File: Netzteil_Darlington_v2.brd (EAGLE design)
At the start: 155.7 x 120 mm, 155 parts, among them IC10 LT4320DIL08, IC11 OPA2197, IC13 OPA2197, IC15 LD33V, IC17 7815TV, IC2 OPA2197, IC4 VXO78012-1000, IC5 LD33V, IC6 VXO7805-1000, IC7 MCP4922, IC8 LTC6102HMS8#PBF, IC9 LM334, T1 IRLL110TRPBF, T10 BC847ALT1G, T11 BC847ALT1G, T12 DMG2302UK-7, T13 DMG2302UK-7, T14 DMG2302UK-7, T2 BC847ALT1G, T3 BD139, T4 2N5401, T5 TIP3055, T6 TIP3055, T7 BD139, T8 BC847ALT1G

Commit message: update to latest version
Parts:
- removed C44: 10µ / C3216X7R1E106M160AB, goujine:1206
- removed C46: 100n, goujine:0805
- removed CRNT_READ: (no value), jumper:JP2
- removed D11: EDZV13B, neumluc:SOD-523
- removed D13: 1N4007, diode:DO214AA
- removed R25: 347k 1%, neumluc:C0805K
- removed R46: 10k, neumluc:C0805K
- removed T8: BC847ALT1G, neumluc:SOT23-BEC
- added C10, C17: 100n/16V, goujine:C0603K
- added C14, C18, C41: 1µ/16V, goujine:0805
- added C21: 330n, goujine:0805
- added C28: 100n, goujine:0805
- added C32, C37: 1µ/50V, goujine:0805
- added C34: 10µ/16V, goujine:0805
- added C40: 100n/50V, goujine:0805
- added IC1: NCP718BSN330T1G, neumluc:SOT23-5
- added IC12: REF5040, neumluc:MSOP8-0.65-3X3MM
- added IC18, IC19: ADS1015, SparkFun-IC-Conversion:MSOP10
- added L6, L8: MPZ2012S601AT000, neumluc:C0805K
- added R13: 10k, neumluc:C0603K
- added R17: 2k2, neumluc:C0805K
- added R19: 1.27R, neumluc:C0805K
- C22, C29: device goujine:0805 -> goujine:C0603K
- C35: value 100n -> 1µ/50V
- C36: value 100n -> 1µ/16V
- C45: value 10µ / C3216X7R1E106M160AB -> 1µ/16V; device goujine:1206 -> goujine:0805
- C7: value 470n -> 100n/16V; device goujine:0805 -> goujine:C0603K
- C8: value 100n -> 10µ/16V
- C9: value 10µ / C3216X7R1E106M160AB -> 100n/16V; device goujine:1206 -> goujine:C0603K
- D4: value MMSD4148T1G opt -> 1N4007; device adafruit:SOD-123 -> diode:DO214AA
- IC17: value 7815TV -> 7818TV
- IC3: value (none) -> DAC8311; device neumluc:SOT23 -> neumluc:SC-70-6
- IC5: value LD33V -> 7815TV; device neumluc:TO220V -> linear:TO220V
- IC7: value MCP4922 -> DAC8311; device neumluc:TSSOP14 -> neumluc:SC-70-6
- IC9: value LM334 -> NCP718BSN330T1G; device neumluc:TO92-G -> neumluc:SOT23-5
- R1: value 1M -> 2k2 5%; device neumluc:C0603K -> neumluc:C0805K
- R12: value 10R 1% -> 10k; device neumluc:C0805K -> neumluc:C0603K
- R2: value 2.4k 0.1% PCF0805-13-2K4BT1 -> 10k 0.1% 10ppm
- R3: value 12k 0.1% ERA-6ARW123V -> 30k 0.1% 10ppm
- R4, R6: value 220R -> 10k; device neumluc:C0805K -> neumluc:C0603K
- R42: value 681k 1% -> 390k 1%; device neumluc:C0603K -> neumluc:C0805K
- T4: value 2N5401 -> DMMT5551-7-F; device neumluc:TO92-G -> neumluc:SOT-26
- moved R6 80.9 mm to (65.2, 39.6), turned to 0 degrees
- moved R4 62.8 mm to (64.3, 41.0)
- moved R1 40.4 mm to (115.7, 57.3), turned to 90 degrees
- moved T4 37.0 mm to (114.8, 61.4), turned to 90 degrees
- moved D4 22.2 mm to (51.3, 60.4), turned to 270 degrees
- moved C25 18.6 mm to (104.6, 61.5)
- moved C26 18.6 mm to (92.7, 54.4)
- moved C47 18.6 mm to (92.9, 51.0)
- moved C48 18.6 mm to (92.4, 61.5)
- moved IC11 18.6 mm to (97.5, 57.7)
- moved R14 18.6 mm to (106.8, 61.5)
- moved R15 18.6 mm to (102.7, 61.5)
- moved R32 18.6 mm to (90.5, 61.5)
- moved R35 18.6 mm to (97.5, 61.6)
- moved R37 18.6 mm to (95.9, 51.9)
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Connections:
- removed net AREF2048: C9.1, IC3.2, IC7.11, IC7.13, U$33.AREF
- removed net CRNT_READ_OP: CRNT_READ.2, IC13.5
- removed net DAC_CS: IC7.3, U$33.14/A0
- removed net DAC_SHDN: IC7.9, U$33.A22/DAC1
- removed net MISO: U$33.12/MISO
- removed net N$39: C44.2, D13.A, IC5.2, L5.1
- new net +27V: C1.+, C12.2, C19.2, C2.+, C21.1, C27.1, C42.1, C53.1, D4.C, D9.C, IC10.6, IC17.1, IC4.1, IC5.1, IC6.1, IC8.7, R5.I2, T15.3, T16.3
- new net +3.3V_A2: C14.2, IC9.5, L6.2
- new net +3.3V_LP: R4.2, R6.1, U$33.3V3_LO
- new net IDAC_CS: IC7.1, U$33.15/A1
- new net N$18: IC19.2, R12.2
- new net N$24: C17.1, IC18.1, IC18.8, L8.1, R13.1
- new net N$25: C37.2, C40.2, IC12.2, L5.1
- new net N$32: C45.1, R19.2
- new net SCL: IC18.10, IC19.10, R4.1, U$33.19/A5/SCL
- new net SDA: IC18.9, IC19.9, R6.2, U$33.18/A4/SDA
- new net VDAC_CS: IC3.1, U$33.14/A0
- new net VREF4096: C34.1, C41.1, C7.1, C8.1, C9.1, IC12.6, IC3.4, IC7.4, R19.1
- net +15V: now also C28.1, C32.2, C35.2, D4.A, IC1.1, IC1.3, IC9.1, IC9.3, L5.2, R1.1, R17.1; no longer C22.1, C29.1, C35.1, C43.1, D13.C, D9.A, IC13.8, IC17.3, IC2.8, R18.1, R46.1, T11.C
- net +18V: now also C22.1, C29.1, C43.1, D9.A, IC13.8, IC17.3, IC2.8, R18.1, T11.C; no longer C1.+, C12.2, C19.2, C2.+, C27.1, C42.1, C53.1, D9.C, IC10.6, IC17.1, IC4.1, IC6.1, IC8.7, R5.I2, T15.3, T16.3
- net +3.3V_A: now also C18.2, IC1.5, L8.2; no longer C36.2, C45.1, C46.1, C7.1, C8.1, IC3.1, IC7.1, L5.2
- net +V_ADJ: now also T4.4; no longer IC9.1, T8.C
- net ADC_CH0: now also IC18.6; no longer U$33.20/A6
- net ADC_CH1: now also IC19.4; no longer U$33.33/A14
- net ADC_CH2: now also IC19.6; no longer U$33.34/A15
- net ADC_CH3: now also IC18.4; no longer U$33.19/A5/SCL
- net AGND: now also C10.2, C14.1, C17.2, C18.1, C21.2, C28.2, C32.1, C34.2, C35.1, C36.2, C37.1, C40.1, C41.2, IC1.2, IC12.4, IC18.3, IC18.5, IC18.7, IC19.1, IC19.3, IC19.5, IC19.7, IC3.5, IC5.2, IC7.5, IC9.2, R17.2, SENSE.1, T4.5, T4.6; no longer C35.2, C36.1, C44.1, C46.2, D11.A, IC3.3, IC5.1, IC7.12, IC7.8, IC9.3, R1.1, R12.2, T8.E
- net BTN_I_DOWN: now also U$33.37/A18; no longer U$33.39/A20
- net BTN_I_UP: now also U$33.36/A17; no longer U$33.38/A19
- net BTN_V_DOWN: now also U$33.35/A16; no longer U$33.37/A18
- net BTN_V_UP: now also U$33.34/A15; no longer U$33.36/A17
- net CRNT_READ: now also IC13.5; no longer CRNT_READ.3
- net CRNT_READ_RAW: no longer CRNT_READ.1
- net ISET: now also IC7.6; no longer IC7.14
- net MOSI: now also IC3.3, IC7.3; no longer IC7.5
- net N$10: no longer D4.C
- net N$11: now also R1.2, T4.1, T4.2, T4.3; no longer R25.1, T8.B
- net N$14: now also C36.1, IC12.5; no longer D11.C, R25.2, R46.2
- net N$15: no longer R4.2
- net N$16: now also IC18.2, R13.2; no longer IC9.2, R12.1
- net N$19: now also C10.1, IC19.8, L6.1, R12.1; no longer R1.2, T4.2
- net N$21: no longer T4.1
- net N$22: no longer D4.A, T4.3
- net N$4: no longer R6.1
- net N$5: no longer R6.2
- net N$8: no longer R4.1
- net SCK: now also IC3.2, IC7.2; no longer IC7.4
- net TH0: now also U$33.33/A14; no longer U$33.35/A16
- net VSET: now also IC3.6; no longer IC7.10
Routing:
- net +27V: track 0.00 -> 188.7 mm, vias 0 -> 86
- net +18V: track 159.4 -> 50.0 mm, vias 85 -> 2
- net SCL: track 0.00 -> 68.0 mm
- net SDA: track 0.00 -> 65.3 mm
- net AREF2048: track 38.4 -> 0.00 mm
- net +3.3V_A: track 40.2 -> 3.80 mm, vias 2 -> 0
- net +V_ADJ: track 21.1 -> 54.8 mm
- net VREF4096: track 0.00 -> 22.2 mm
- net AGND: track 87.5 -> 109.3 mm, vias 34 -> 45
- net N$8: track 23.7 -> 5.19 mm, vias 1 -> 0
- net SCK: track 28.8 -> 47.3 mm
- net N$4: track 23.7 -> 5.19 mm, vias 1 -> 0
- net TH0: track 46.5 -> 64.8 mm, vias 6 -> 4
- net +15V: track 171.3 -> 153.4 mm, vias 9 -> 10
- net VDAC_CS: track 0.00 -> 17.9 mm, vias 0 -> 2
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- added copper zone on layer 1, net +27V
- added copper zone on layer 16, net +27V
- removed copper zone on layer 1, net +18V
- removed copper zone on layer 16, net +18V
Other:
- board size 155.7 x 120 mm -> 156 x 120 mm
- board text removed: "HS: ATS-52350P-C1-R0 ATS-54350R-C1-R0"

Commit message: update to latest version
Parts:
- removed BTNS: (no value), con-lstb:MA05-1
- added I: (no value), con-lstb:MA03-1
- added SENSE_GND, V: (no value), jumper:JP1
- moved H4 46.1 mm to (135.8, 67.3)
- moved VOUT 39.2 mm to (113.4, 53.8)
- moved GND_OUT_CON 30.9 mm to (135.0, 53.8)
- moved D6 26.5 mm to (110.9, 67.1), turned to 180 degrees
- moved REL1 23.8 mm to (124.2, 48.7)
- moved D8 23.7 mm to (124.0, 32.1)
- moved R1 22.7 mm to (98.0, 71.5), turned to 270 degrees
- moved T1 22.1 mm to (120.4, 24.8), turned to 180 degrees
- moved R31 20.8 mm to (123.7, 20.9), turned to 270 degrees
- moved VSS 18.4 mm to (47.4, 2.73)
- moved C16 17.8 mm to (120.7, 9.63)
- moved IC4 17.8 mm to (125.3, 8.52)
- moved L4 17.8 mm to (125.3, 14.2)
- moved T4 16.9 mm to (99.0, 67.3), turned to 270 degrees
- moved H3 16.6 mm to (135.8, 19.7)
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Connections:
- new net SENSE_GND: IC19.5, SENSE_GND.1, SENSE_GND.2
- net +V_ADJ: now also REL1.S1; no longer REL1.P1
- net AGND: now also I.3, REL1.S2; no longer BTNS.5, IC19.5, REL1.P2, SENSE.1
- net BTN_I_DOWN: now also I.2, U$33.17/A3; no longer BTNS.4, U$33.37/A18
- net BTN_I_UP: now also I.1, U$33.16/A2; no longer BTNS.3, U$33.36/A17
- net BTN_V_DOWN: now also V.2; no longer BTNS.2
- net BTN_V_UP: now also V.1; no longer BTNS.1
- net GND_OUT_CON: now also REL1.P2; no longer REL1.S2
- net SENSE: now also SENSE.1
- net V_OUT_CON: now also REL1.P1; no longer REL1.S1
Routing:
- net REL-OUT: track 47.9 -> 25.2 mm
- net +12V: track 55.4 -> 36.0 mm
- net +27V: track 188.7 -> 173.2 mm
- net N$22: track 74.6 -> 63.1 mm
- net TH0: track 64.8 -> 53.4 mm
- net SENSE_GND: track 0.00 -> 11.1 mm
- net SCL: track 68.0 -> 59.3 mm
- net SDA: track 65.3 -> 57.6 mm
- net BTN_V_DOWN: track 3.57 -> 11.1 mm
- net +V_ADJ: track 54.8 -> 61.2 mm
- net +15V: track 153.4 -> 147.4 mm
- net VDAC_CS: track 17.9 -> 13.0 mm
- net IDAC_CS: track 17.7 -> 12.8 mm
- net N$37: track 4.30 -> 8.90 mm
- net N$5: track 41.3 -> 36.8 mm
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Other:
- board size 156 x 120 mm -> 141 x 115.5 mm

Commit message: Update to v1.9
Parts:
- removed C29: 100n, goujine:C0603K
- removed C50: 10n, goujine:0805
- removed D12: 1N4007, diode:DO214AA
- removed DSPLY2, LED, SENSE, SENSE_GND, V: (no value), jumper:JP1
- removed DSPLY_LED: (no value), neumluc:MA03-1
- removed ESP: (no value), con-lstb:MA06-1
- removed I: (no value), con-lstb:MA03-1
- removed IC11, IC13: OPA2197, goujine:SOP8
- removed R15: 10.1k 0.1% RN732ATTD1012B25, neumluc:C0805K
- removed R31: 360R, neumluc:C0805K
- removed R38: 4.7k, neumluc:C0805K
- removed R39: 100R, neumluc:C0805K
- removed T10: BC847ALT1G, neumluc:SOT23-BEC
- added BTN, SV1, SV2: (no value), neumluc:JST-PH-2.0-2P
- added C33, C44: 100µ/50V, goujine:C+/3.5/8
- added ESP/BTNS: (no value), neumluc:JST-PH-2.0-8P
- added IC14: QUAD-OPVOPA4197, neumluc:SO14
- added KK2: D01S, heatsink:D01S
- added R25, R26: 1k 1% 1/8W, neumluc:C0805K
- added SINK: (no value), jumper:JP1
- added SV5: (no value), neumluc:JST-PH-2.0-5P
- C1, C2: value UVZ1H103MRD -> 10000µ/50V
- C10, C17, C7, C9: device goujine:C0603K -> goujine:0805
- C11: value 330n opt -> 330n opt/50V
- C13: value 100n opt -> 100n opt/50V
- C15: value 100µ/50V EEU-FR1H101 -> 100µ/50V
- C16: value 10µ/16V -> 10µ/25V; device we-rcl:C1210 -> goujine:1206
- C20: device we-rcl:C1210 -> goujine:1206
- C21, C42: value 330n -> 330n/50V
- C22: value 100n -> 100n/35V; device goujine:C0603K -> goujine:0805
- C23, C30, C39, C49: value 10µ / C3216X7R1E106M160AB -> 10µ/16V
- C24, C3, C31, C38, C48: value 100n -> 100n/16V
- C25, C28, C43: value 100n -> 100n/35V
- C26: value 100n -> 1n/50V
- C27: value 100n -> 100n/50V
- C32, C35, C37: value 1µ/50V -> 1µ/35V
- C34, C8: device goujine:0805 -> goujine:1206
- C4: value 10n -> 10n/50V
- C40: value 100n/50V -> 100n/35V
- C47, C51: value 10n -> 10n/16V
- C5: value 1n -> 1n/50V
- C52: value 22p opt -> 22p opt/35V C0G
- C53: value (none) -> 1µ/50V
- C6: value 22pF -> 22pF/35V C0G
- D14, D6: value CDBA5200-HF -> CGRB307-G; device neumluc:DO214AC-2 -> neumluc:DO214AA-CGRB307-G
- D4, D8, D9: value 1N4007 -> CGRB307-G; device diode:DO214AA -> neumluc:DO214AA-CGRB307-G
- DSPLY: device con-lstb:MA07-1 -> neumluc:JST-PH-2.0-7P
- ENC: device con-lstb:MA03-1 -> neumluc:JST-PH-2.0-3P
- FAN: device con-lstb:MA04-1 -> neumluc:JST-PH-2.0-4P
- IC18, IC19: value ADS1015 -> ADS1115; device SparkFun-IC-Conversion:MSOP10 -> neumluc:MSOP10
- IC2: value OPA2197 -> (none)
- R1: value 2k2 5% -> 12k 0.5% 50 ppm 1/10W
- R10: value 4.7k opt -> 4.7k opt 1% 1/10W
- R11, R16: value 22R -> 22R 5% 1/10W
- R12: value 10k -> 221R 0.5% 50ppm 1/10W; device neumluc:C0603K -> neumluc:C0805K
- R13: value 10k -> 1k 0.5% 50 ppm 1/10W; device neumluc:C0603K -> neumluc:C0805K
- R14: value 90.9k 0.1% RN73C2A90K9BTDF -> 10R 0.5% 50 ppm 1/4W
- R17: value 2k2 -> 2k2 5% 1/8W
- R18: value 2k2 -> 1k 1% 1/8W
- R19: value 1.27R -> 1.27R 1% 1/10W
- R20, R21: value 0R1 0.5% -> 0R1 0.5% 7W
- R22, R32: value 10.1k 0.1% RN732ATTD1012B25 -> 10.1k 0.1% 10ppm 1/10W
- R23, R30: value 90.9k 0.1% RN73C2A90K9BTDF -> 90.9k 0.1% 10ppm 1/10W
- R24: value 1k opt -> 1k 1% 1/10W
- R28, R29: value 220R -> 220R 5% 1/10W
- R35, R40: value 4.7k -> 4.7k 5% 1/10W
- R37: value 100R -> 2.2k 5% 1/8W
- R4, R6: value 10k -> 10k 5% 1/10W; device neumluc:C0603K -> neumluc:C0805K
- R41: value 100R -> 100R 5% 1/10W
- R42: value 390k 1% -> 65k 1% 1/10W
- R43: value 5k 0.1% low ppm TNPW12065K00BEEN -> 5k 0.1% 25ppm
- R44, R45: value 100R 0.1% low ppm PCF0805-13-100RBT1 -> 100R 0.1% 5ppm 1/10W
- R48, R7: value 10k -> 10k 5% 1/10W
- R5: value 10m -> 10m 0.1% 15ppm 0.5W
- R8: value 47k -> 47k 1% 1/10W
- R9: value 4.7k -> 4.7k 1% 1/10W
- T1: value IRLL110TRPBF -> PMV130ENEAR; device goujine:SOT223-4 -> neumluc:SOT23
- T12, T13, T14: value DMG2302UK-7 -> PMV130ENEAR
- T15, T16, T17, T18: value (none) -> IRFR7546TRPBF
- T4: value DMMT5551-7-F -> PMV130ENEAR; device neumluc:SOT-26 -> neumluc:SOT23
- moved R13 35.2 mm to (97.9, 54.3), turned to 270 degrees
- moved VSS 35.1 mm to (82.3, 5.74)
- moved C32 26.1 mm to (81.3, 45.7)
- moved R1 21.6 mm to (97.2, 49.8), turned to 90 degrees
- moved IC9 20.5 mm to (84.0, 44.9), turned to 180 degrees
- moved C13 20.3 mm to (102.6, 56.5), turned to 270 degrees
- moved C25 19.6 mm to (83.3, 50.6), turned to 180 degrees
- moved D14 16.8 mm to (111.9, 66.1)
- moved C14 15.1 mm to (86.7, 44.3), turned to 270 degrees
- moved IC2 15.0 mm to (87.2, 54.3)
- moved AGND 14.9 mm to (129.5, 59.1)
- moved T4 14.0 mm to (94.9, 54.0), turned to 0 degrees
- moved C42 13.4 mm to (43.0, 62.5), turned to 270 degrees
- moved C22 12.9 mm to (62.1, 67.0), turned to 90 degrees
- moved D6 12.7 mm to (106.1, 55.3), turned to 270 degrees
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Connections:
- removed net ADC_CH1: C50.1, IC19.4, R39.2
- removed net ADC_SENSE: C25.1, IC11.3, R14.1, R15.2
- removed net N$12: D8.A, REL1.+, T1.2, T1.4
- removed net N$37: R31.1, R48.2, T1.1
- removed net N$40: IC11.7, T2.B
- removed net N$42: IC11.1, T10.B
- removed net N$43: IC11.2, R38.1, R39.1, T10.E
- removed net N$44: IC13.7, T11.B
- removed net SENSE: R14.2, SENSE.1, SENSE.2
- removed net SENSE_GND: IC19.5, SENSE_GND.1, SENSE_GND.2
- new net 3.3V_A2_FILTERED: C10.1, IC19.8, L6.1, R1.1, SV1.2
- new net 3.3V_TH: R42.1, SV2.2
- new net N$26: R18.2, R25.1
- new net N$30: R25.2, R26.1
- new net N$31: C6.1, IC14.9, R2.2, R3.2, R8.2
- new net N$33: C26.1, IC2.1, T4.1
- new net N$34: SINK.2, T4.3
- new net N$38: D8.A, REL1.+, T1.3
- new net TH0_ADC: IC19.4, SV1.1
- net +15V: now also C25.1, IC2.8; no longer C26.1, IC11.8, R1.1, R42.1, T10.C
- net +18V: now also IC14.4; no longer C29.1, IC13.8, IC2.8
- net +27V: now also C33.+, C44.+
- net +3.3V: now also DSPLY.6, ESP/BTNS.4; no longer DSPLY.2, DSPLY2.2, ESP.4
- net +5V_INT_D: no longer D12.C
- net +V_ADJ: now also SINK.1; no longer T4.4
- net ADC_CH0: now also IC18.4; no longer IC18.6
- net ADC_CH3: now also IC18.6; no longer IC18.4
- net ADC_VOUT: now also IC2.5; no longer IC11.5
- net AGND: now also IC14.11, R12.2, R14.2, R26.2, U$33.GND2; no longer C26.2, C29.2, C50.2, I.3, IC11.4, IC13.4, R15.1, R18.2, R38.2, T4.5, T4.6
- net BTN_I_DOWN: now also BTN.2; no longer I.2
- net BTN_I_UP: now also BTN.1; no longer I.1
- net BTN_V_DOWN: now also ESP/BTNS.8, U$33.33/A14; no longer U$33.35/A16, V.2
- net BTN_V_UP: now also ESP/BTNS.7; no longer V.1
- net CRNT_READ: now also IC14.13, IC14.5; no longer IC13.5, IC2.6
- net DSPLY_CS: now also DSPLY.1; no longer DSPLY.7
- net DSPLY_DC: now also DSPLY.5; no longer DSPLY.3
- net DSPLY_RST: now also DSPLY.2; no longer DSPLY.6
- net ESP-IO: now also ESP/BTNS.5, U$33.35/A16; no longer ESP.5, U$33.10/CS
- net ESP-RST: now also ESP/BTNS.3; no longer ESP.3
- net ESP-RX: now also ESP/BTNS.2, U$33.32/A13; no longer ESP.2, U$33.31/A12
- net ESP-TX: now also ESP/BTNS.1, U$33.31/A12; no longer ESP.1, U$33.32/A13
- net ISET: now also IC14.12; no longer IC2.5
- net MOSI: now also DSPLY.3; no longer DSPLY.5
- net N$11: now also IC2.3, R12.1; no longer T4.1, T4.2, T4.3
- net N$16: now also R14.1, T4.2; no longer IC18.2
- net N$18: now also C26.2, IC2.2, R13.1; no longer IC19.2, R12.2
- net N$19: now also IC2.7, T2.B; no longer C10.1, IC19.8, L6.1, R12.1
- net N$20: now also SV5.1; no longer LED.1
- net N$21: now also IC14.8; no longer IC2.1
- net N$23: now also SV5.2; no longer LED.2
- net N$24: no longer R13.1
- net N$35: no longer D12.A
- net N$41: now also IC2.6; no longer IC11.6
- net N$45: now also IC14.6; no longer IC13.6
- net N$46: now also SV5.4; no longer DSPLY_LED.2
- net N$48: now also SV5.5; no longer DSPLY_LED.3
- net N$6: now also IC14.7, T11.B; no longer C6.1, IC2.2, R2.2, R3.2, R8.2
- net N$7: now also SV5.3; no longer DSPLY_LED.1
- net OVRCRNT_DET: now also IC14.14, IC14.3; no longer IC13.3, IC2.7
- net OVRCRNT_DET_BUF: now also IC14.1, IC14.2; no longer IC13.1, IC13.2
- net REL-OUT: now also R48.2, T1.1; no longer R31.2
- net TH0: now also SV2.1; no longer U$33.33/A14
- net VSET: now also IC14.10; no longer IC2.3
- net VSS: now also C33.-, C44.-, DSPLY.7, ESP/BTNS.6, T1.2; no longer DSPLY.1, DSPLY2.1, ESP.6, T1.3
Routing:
- net +15V: track 147.4 -> 65.7 mm, vias 10 -> 4
- net TH0: track 53.4 -> 9.82 mm, vias 4 -> 0
- net ESP-IO: track 49.1 -> 18.1 mm
- net +27V: track 173.2 -> 144.7 mm
- net +V_ADJ: track 61.2 -> 33.7 mm
- net +18V: track 48.3 -> 28.6 mm
- net AGND: track 107.8 -> 89.3 mm, vias 44 -> 46
- net 3.3V_A2_FILTERED: track 0.00 -> 18.2 mm
- net N$43: track 13.6 -> 0.00 mm
- net N$22: track 63.1 -> 50.8 mm, vias 2 -> 0
- net N$11: track 4.22 -> 15.6 mm
- net SENSE_GND: track 11.1 -> 0.00 mm
- net N$3: track 70.3 -> 59.3 mm
- net CRNT_READ: track 28.7 -> 18.7 mm
- net N$12: track 8.91 -> 0.00 mm
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- added copper zone on layer 1, net AGND
- added copper zone on layer 1, net CRNT_READ
- added copper zone on layer 1, net CRNT_READ_RAW
- added copper zone on layer 1, net N$13
- removed copper zone on layer 1, net N$12
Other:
- board size 141 x 115.5 mm -> 141 x 109.9 mm
- board text added: "3.3V"
- board text added: "A"
- board text added: "B"
- board text added: "B1"
- board text added: "B2"
- board text added: "BTN"
- board text added: "IO"
- board text added: "I_DWN"
- board text added: "I_UP"
- board text added: "LED 1"
- board text added: "LED 2"
- board text added: "Netzteil_Darlington_v2 Rev 1.9"
- board text added: "R G B"
- board text added: "RST"
- board text added: "RX"
- board text added: "TX"
- board text added: "VSS"
- board text removed: "Netzteil_Darlington_v2 Rev 1.8"

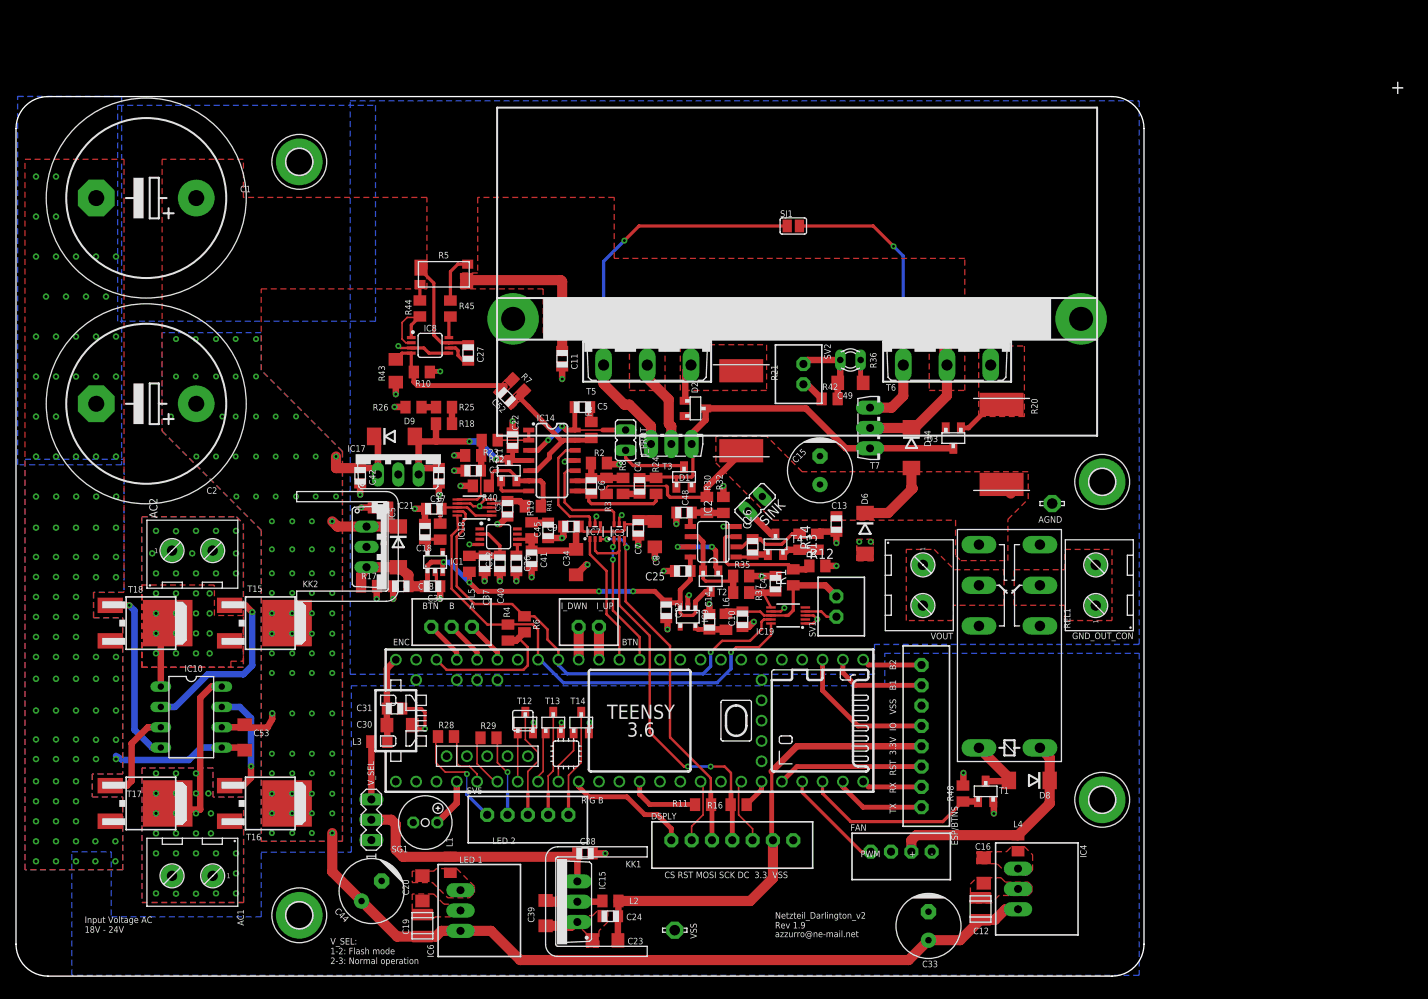
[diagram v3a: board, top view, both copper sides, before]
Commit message: repair designators, add gerber files
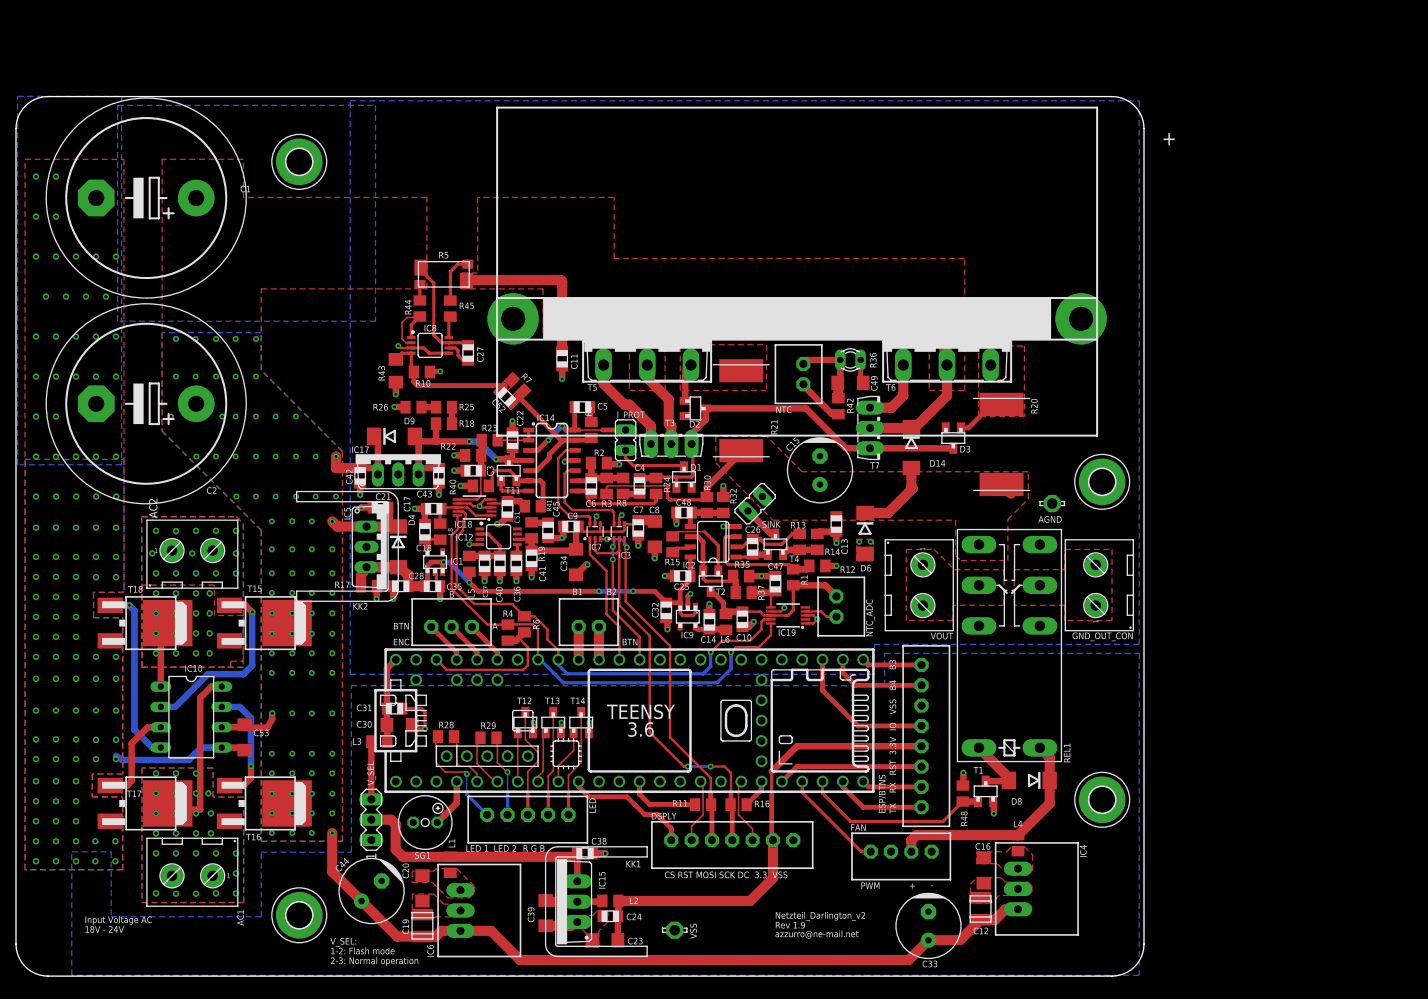
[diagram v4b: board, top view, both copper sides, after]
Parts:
- removed SJ1: (no value), jumper:SJ
- added R15: 1k5 5% 1/8W, neumluc:C0805K
- IC2: value (none) -> OPA2197
- R37: value 2.2k 5% 1/8W -> 2.2k 5% 1/10W
- R41: value 100R 5% 1/10W -> 2.2k 5% 1/10W
- R42: value 65k 1% 1/10W -> 64.9k 1% 1/10W
- moved R42 1.42 mm to (102.8, 71.2), turned to 90 degrees
- moved C25 0.63 mm to (83.3, 50.0)
- moved R37 0.32 mm to (91.0, 47.9)
- renumbered SV1 to NTC_ADC, SV2 to NTC, SV5 to LED
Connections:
- net BTN_I_DOWN renamed BTN1
- net BTN_I_UP renamed BTN2
- net BTN_V_DOWN renamed BTN3
- net BTN_V_UP renamed BTN4
- new net N$12: IC2.7, R15.2
- net +15V: no longer T2.C
- net 3.3V_A2_FILTERED: now also T2.C
- net N$15: no longer SJ1.1
- net N$19: now also R15.1; no longer IC2.7
- net N$5: no longer SJ1.2
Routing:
- net N$15: track 50.4 -> 12.7 mm, vias 1 -> 0
- net N$5: track 36.8 -> 8.62 mm, vias 1 -> 0
- net 3.3V_A2_FILTERED: track 18.2 -> 21.9 mm
- net +15V: track 65.7 -> 62.7 mm
- net 3.3V_TH: track 3.04 -> 6.01 mm
- net N$12: track 0.00 -> 2.51 mm
- net N$19: track 9.18 -> 9.86 mm, vias 2 -> 0
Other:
- board text added: "B3"
- board text added: "B4"
- board text removed: "I_DWN"
- board text removed: "I_UP"
